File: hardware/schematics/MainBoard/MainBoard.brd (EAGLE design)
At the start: 80 x 107.6 mm, 17 parts

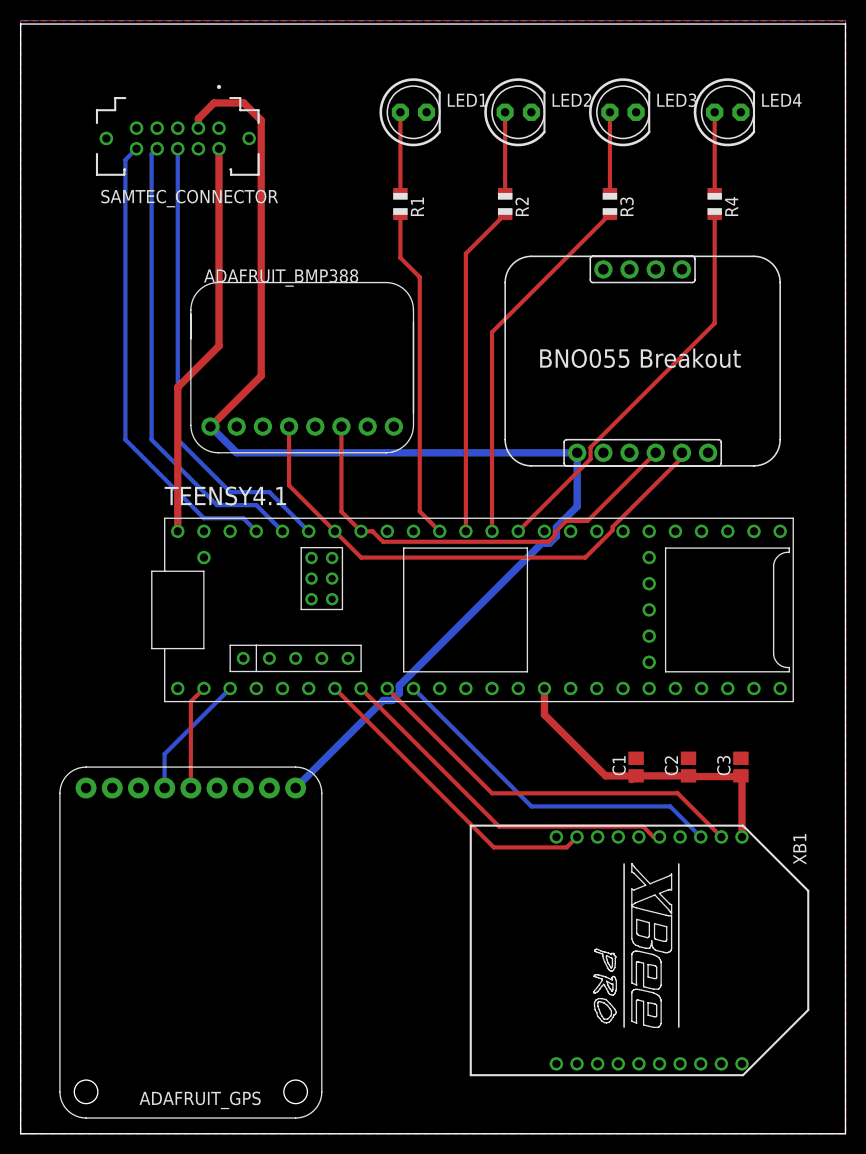
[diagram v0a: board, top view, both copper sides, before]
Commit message: Add Power Board | Change MB Connector Pins | Move Old PDB.sch to PCBs Folder
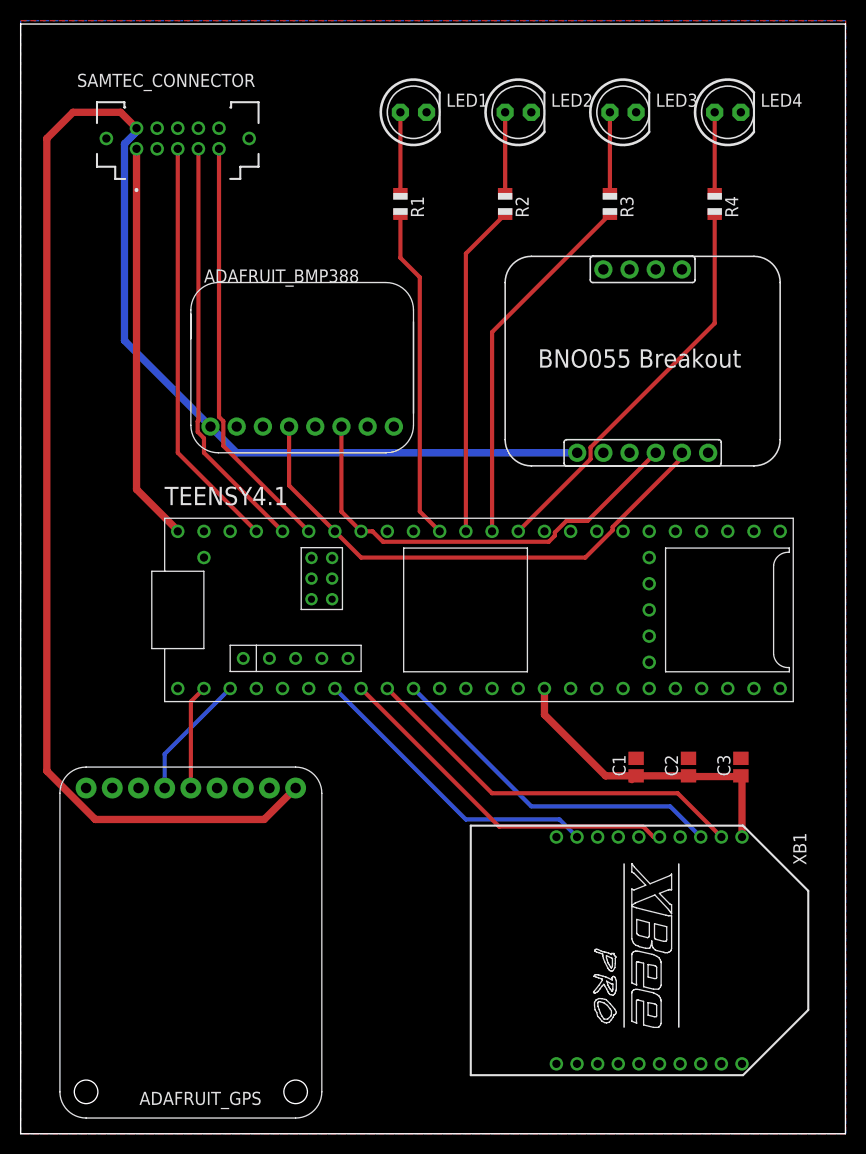
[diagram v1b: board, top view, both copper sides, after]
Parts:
- turned SAMTEC_CONNECTOR to 0 degrees
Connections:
- net 3V3: now also SAMTEC_CONNECTOR.02; no longer SAMTEC_CONNECTOR.03
- net 5V: now also SAMTEC_CONNECTOR.01; no longer SAMTEC_CONNECTOR.02
- net BATT_TEMP: now also SAMTEC_CONNECTOR.05, TEENSY4.1.D23/A9; no longer SAMTEC_CONNECTOR.06, TEENSY4.1.D21/A7
- net GND: now also SAMTEC_CONNECTOR.03, SAMTEC_CONNECTOR.06, SAMTEC_CONNECTOR.08, SAMTEC_CONNECTOR.10; no longer SAMTEC_CONNECTOR.01, SAMTEC_CONNECTOR.05, SAMTEC_CONNECTOR.07, SAMTEC_CONNECTOR.09
- net I_SENSE: now also SAMTEC_CONNECTOR.09, TEENSY4.1.D21/A7; no longer SAMTEC_CONNECTOR.08, TEENSY4.1.D22/A8
- net V_BATT: now also SAMTEC_CONNECTOR.07, TEENSY4.1.D22/A8; no longer SAMTEC_CONNECTOR.10, TEENSY4.1.D23/A9
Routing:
- net 3V3: track 153.2 -> 200.3 mm
- net V_BATT: track 45.0 -> 40.5 mm
- net BATT_TEMP: track 44.6 -> 40.3 mm
- net I_SENSE: track 44.8 -> 40.7 mm
- net XBEE_EN: track 30.3 -> 29.4 mm
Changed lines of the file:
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@@
 <drawing>
 <settings>
-<setting alwaysvectorfont="yes"/>
+<setting alwaysvectorfont="no"/>
 <setting verticaltext="up"/>
 </settings>
@@
 <attribute name="VALUE" x="20.066" y="5.842" size="1.27" layer="27" rot="R180"/>
 </element>
-<element name="SAMTEC_CONNECTOR" library="T2M-105-01-X-D-TH-WT" package="SAMTEC_T2M-105-01-X-D-TH-WT" value="T2M-105-01-X-D-TH-WT" x="15.24" y="96.52" smashed="yes" rot="R180">
-<attribute name="MANUFACTURER" value="Samtec" x="-39.37" y="166.37" size="1.778" layer="27" rot="R180" display="off"/>
-<attribute name="MAXIMUM_PACKAGE_HEIGHT" value="6.55mm" x="-39.37" y="166.37" size="1.778" layer="27" rot="R180" display="off"/>
-<attribute name="NAME" x="25.01" y="91.52" size="1.27" layer="25" rot="R180"/>
-<attribute name="PARTREV" value="AH" x="-39.37" y="166.37" size="1.778" layer="27" rot="R180" display="off"/>
-<attribute name="STANDARD" value="Manufacturer Recommendations" x="-39.37" y="166.37" size="1.778" layer="27" rot="R180" display="off"/>
-<attribute name="VALUE" x="23.74" y="102.02" size="1.27" layer="27" rot="R180" align="top-left"/>
+<element name="SAMTEC_CONNECTOR" library="T2M-105-01-X-D-TH-WT" package="SAMTEC_T2M-105-01-X-D-TH-WT" value="T2M-105-01-X-D-TH-WT" x="15.24" y="96.52" smashed="yes">
+<attribute name="MANUFACTURER" value="Samtec" x="69.85" y="26.67" size="1.778" layer="27" display="off"/>
+<attribute name="MAXIMUM_PACKAGE_HEIGHT" value="6.55mm" x="69.85" y="26.67" size="1.778" layer="27" display="off"/>
+<attribute name="NAME" x="5.47" y="101.52" size="1.27" layer="25"/>
+<attribute name="PARTREV" value="AH" x="69.85" y="26.67" size="1.778" layer="27" display="off"/>
+<attribute name="STANDARD" value="Manufacturer Recommendations" x="69.85" y="26.67" size="1.778" layer="27" display="off"/>
+<attribute name="VALUE" x="6.74" y="91.02" size="1.27" layer="27" align="top-left"/>
 </element>
 <element name="LED1" library="adafruit(seeIMUBreakout)" package="LED5MM" value="" x="38.1" y="99.06" smashed="yes">
@@
 <vertex x="0" y="0"/>
 </polygon>
-<contactref element="SAMTEC_CONNECTOR" pad="05"/>
-<contactref element="SAMTEC_CONNECTOR" pad="09"/>
-<contactref element="SAMTEC_CONNECTOR" pad="07"/>
-<contactref element="SAMTEC_CONNECTOR" pad="01"/>
+<contactref element="SAMTEC_CONNECTOR" pad="06"/>
+<contactref element="SAMTEC_CONNECTOR" pad="08"/>
+<contactref element="SAMTEC_CONNECTOR" pad="10"/>
+<contactref element="SAMTEC_CONNECTOR" pad="03"/>
 </signal>
 <signal name="AGND">
@@
 <signal name="5V">
 <contactref element="TEENSY4.1" pad="5V"/>
-<contactref element="SAMTEC_CONNECTOR" pad="02"/>
 <contactref element="TEENSY4.1" pad="VIN"/>
-<wire x1="19.24" y1="95.52" x2="19.24" y2="76.39" width="0.7112" layer="1"/>
-<wire x1="15.24" y1="72.39" x2="15.24" y2="58.42" width="0.7112" layer="1"/>
-<wire x1="19.24" y1="76.39" x2="15.24" y2="72.39" width="0.7112" layer="1"/>
+<contactref element="SAMTEC_CONNECTOR" pad="01"/>
+<wire x1="11.24" y1="95.52" x2="11.24" y2="62.5" width="0.7112" layer="1"/>
+<wire x1="15.24" y1="58.5" x2="11.24" y2="62.5" width="0.7112" layer="1"/>
+<wire x1="15.24" y1="58.5" x2="15.24" y2="58.42" width="0.7112" layer="1"/>
 <wire x1="21.59" y1="46.1" x2="15.24" y2="58.42" width="0" layer="19" extent="1-1"/>
 </signal>
@@
 <wire x1="64.77" y1="34.71" x2="59.69" y2="34.71" width="0.7112" layer="1"/>
 <wire x1="59.69" y1="34.71" x2="56.73" y2="34.71" width="0.7112" layer="1"/>
-<contactref element="SAMTEC_CONNECTOR" pad="03"/>
 <contactref element="U$1" pad="VIN"/>
-<wire x1="18.7559875" y1="99.9585" x2="17.24" y2="98.4425125" width="0.7112" layer="1"/>
-<wire x1="17.24" y1="97.52" x2="17.24" y2="98.4425125" width="0.7112" layer="1"/>
-<wire x1="18.7559875" y1="99.9585" x2="21.6490125" y2="99.9585" width="0.7112" layer="1"/>
-<wire x1="21.6490125" y1="99.9585" x2="23.3335" y2="98.2740125" width="0.7112" layer="1"/>
-<wire x1="23.3335" y1="98.2740125" x2="23.3335" y2="73.4985" width="0.7112" layer="1"/>
-<wire x1="18.415" y1="68.58" x2="23.3335" y2="73.4985" width="0.7112" layer="1"/>
-<wire x1="18.415" y1="68.58" x2="20.955" y2="66.04" width="0.7112" layer="16"/>
-<wire x1="20.955" y1="66.04" x2="53.975" y2="66.04" width="0.7112" layer="16"/>
 <contactref element="TEENSY4.1" pad="3.3V"/>
 <wire x1="50.8" y1="43.18" x2="50.8" y2="40.64" width="0.7112" layer="1"/>
 <wire x1="56.73" y1="34.71" x2="50.8" y2="40.64" width="0.7112" layer="1"/>
-<wire x1="53.975" y1="60.833" x2="53.975" y2="66.04" width="0.7112" layer="16"/>
-<wire x1="26.67" y1="33.528" x2="35.16" y2="42.018" width="0.7112" layer="16"/>
-<wire x1="35.16" y1="42.018" x2="36.04131875" y2="42.018" width="0.7112" layer="16"/>
-<wire x1="36.04131875" y1="42.018" x2="36.722" y2="42.69868125" width="0.7112" layer="16"/>
-<wire x1="51.28131875" y1="57.258" x2="51.962" y2="57.93868125" width="0.7112" layer="16"/>
-<wire x1="51.962" y1="57.93868125" x2="51.962" y2="58.82" width="0.7112" layer="16"/>
-<wire x1="51.962" y1="58.82" x2="53.975" y2="60.833" width="0.7112" layer="16"/>
-<wire x1="36.722" y1="42.69868125" x2="36.722" y2="43.44531875" width="0.7112" layer="16"/>
-<wire x1="36.722" y1="43.44531875" x2="50.53468125" y2="57.258" width="0.7112" layer="16"/>
-<wire x1="50.53468125" y1="57.258" x2="51.28131875" y2="57.258" width="0.7112" layer="16"/>
+<contactref element="SAMTEC_CONNECTOR" pad="02"/>
+<wire x1="11.24" y1="97.52" x2="9.7" y2="99.06" width="0.7112" layer="1"/>
+<wire x1="9.7" y1="99.06" x2="5.08" y2="99.06" width="0.7112" layer="1"/>
+<wire x1="2.54" y1="96.52" x2="5.08" y2="99.06" width="0.7112" layer="1"/>
+<wire x1="26.67" y1="33.528" x2="23.622" y2="30.48" width="0.7112" layer="1"/>
+<wire x1="7.2427375" y1="30.48" x2="2.54" y2="35.1827375" width="0.7112" layer="1"/>
+<wire x1="2.54" y1="35.1827375" x2="2.54" y2="96.52" width="0.7112" layer="1"/>
+<wire x1="23.622" y1="30.48" x2="7.2427375" y2="30.48" width="0.7112" layer="1"/>
+<wire x1="11.24" y1="97.52" x2="11.24" y2="97.1725125" width="0.7112" layer="16"/>
+<wire x1="11.24" y1="97.1725125" x2="10.0715" y2="96.0040125" width="0.7112" layer="16"/>
+<wire x1="10.0715" y1="96.0040125" x2="10.0715" y2="76.9235" width="0.7112" layer="16"/>
+<wire x1="10.0715" y1="76.9235" x2="18.415" y2="68.58" width="0.7112" layer="16"/>
+<wire x1="18.415" y1="68.58" x2="20.955" y2="66.04" width="0.7112" layer="16"/>
+<wire x1="20.955" y1="66.04" x2="53.975" y2="66.04" width="0.7112" layer="16"/>
 <wire x1="53.975" y1="66.04" x2="50.8" y2="43.18" width="0" layer="19" extent="1-1"/>
 </signal>
@@
 <contactref element="XB1" pad="9"/>
 <contactref element="TEENSY4.1" pad="D5"/>
-<wire x1="45.8896" y1="27.7704" x2="30.48" y2="43.18" width="0.4064" layer="1"/>
-<wire x1="53.96" y1="28.78" x2="52.9504" y2="27.7704" width="0.4064" layer="1"/>
-<wire x1="52.9504" y1="27.7704" x2="45.8896" y2="27.7704" width="0.4064" layer="1"/>
+<wire x1="30.48" y1="43.18" x2="43.18" y2="30.48" width="0.4064" layer="16"/>
+<wire x1="52.26" y1="30.48" x2="53.96" y2="28.78" width="0.4064" layer="16"/>
+<wire x1="43.18" y1="30.48" x2="52.26" y2="30.48" width="0.4064" layer="16"/>
 </signal>
 <signal name="N$8">
@@
 </signal>
 <signal name="V_BATT">
-<contactref element="TEENSY4.1" pad="D23/A9"/>
-<contactref element="SAMTEC_CONNECTOR" pad="10"/>
-<wire x1="10.16" y1="94.44" x2="11.24" y2="95.52" width="0.4064" layer="16"/>
-<wire x1="22.86" y1="58.42" x2="21.59" y2="59.69" width="0.4064" layer="16"/>
-<wire x1="21.59" y1="59.69" x2="17.78" y2="59.69" width="0.4064" layer="16"/>
-<wire x1="17.78" y1="59.69" x2="10.16" y2="67.31" width="0.4064" layer="16"/>
-<wire x1="10.16" y1="67.31" x2="10.16" y2="94.44" width="0.4064" layer="16"/>
+<contactref element="SAMTEC_CONNECTOR" pad="07"/>
+<contactref element="TEENSY4.1" pad="D22/A8"/>
+<wire x1="17.1704" y1="69.09553125" x2="17.1704" y2="68.06446875" width="0.4064" layer="1"/>
+<wire x1="17.1704" y1="68.06446875" x2="17.78" y2="67.45486875" width="0.4064" layer="1"/>
+<wire x1="17.78" y1="67.45486875" x2="17.78" y2="66.04" width="0.4064" layer="1"/>
+<wire x1="17.24" y1="95.52" x2="17.24" y2="69.16513125" width="0.4064" layer="1"/>
+<wire x1="17.24" y1="69.16513125" x2="17.1704" y2="69.09553125" width="0.4064" layer="1"/>
+<wire x1="17.78" y1="66.04" x2="25.4" y2="58.42" width="0.4064" layer="1"/>
 </signal>
 <signal name="SDA">
@@
 </signal>
 <signal name="I_SENSE">
-<contactref element="TEENSY4.1" pad="D22/A8"/>
-<contactref element="SAMTEC_CONNECTOR" pad="08"/>
-<wire x1="25.4" y1="58.42" x2="22.86" y2="60.96" width="0.4064" layer="16"/>
-<wire x1="19.05" y1="60.96" x2="12.7" y2="67.31" width="0.4064" layer="16"/>
-<wire x1="12.7" y1="67.31" x2="12.7" y2="94.98" width="0.4064" layer="16"/>
-<wire x1="12.7" y1="94.98" x2="13.24" y2="95.52" width="0.4064" layer="16"/>
-<wire x1="22.86" y1="60.96" x2="19.05" y2="60.96" width="0.4064" layer="16"/>
+<contactref element="SAMTEC_CONNECTOR" pad="09"/>
+<contactref element="TEENSY4.1" pad="D21/A7"/>
+<wire x1="19.6596" y1="69.09553125" x2="19.24" y2="69.51513125" width="0.4064" layer="1"/>
+<wire x1="19.24" y1="69.51513125" x2="19.24" y2="95.52" width="0.4064" layer="1"/>
+<wire x1="27.94" y1="58.42" x2="19.6596" y2="66.7004" width="0.4064" layer="1"/>
+<wire x1="19.6596" y1="66.7004" x2="19.6596" y2="69.09553125" width="0.4064" layer="1"/>
 </signal>
 <signal name="BATT_TEMP">
-<contactref element="TEENSY4.1" pad="D21/A7"/>
-<contactref element="SAMTEC_CONNECTOR" pad="06"/>
-<wire x1="15.24" y1="95.52" x2="15.24" y2="67.31" width="0.4064" layer="16"/>
-<wire x1="15.24" y1="67.31" x2="20.32" y2="62.23" width="0.4064" layer="16"/>
-<wire x1="24.13" y1="62.23" x2="27.94" y2="58.42" width="0.4064" layer="16"/>
-<wire x1="20.32" y1="62.23" x2="24.13" y2="62.23" width="0.4064" layer="16"/>
+<contactref element="SAMTEC_CONNECTOR" pad="05"/>
+<contactref element="TEENSY4.1" pad="D23/A9"/>
+<wire x1="15.24" y1="66.04" x2="22.86" y2="58.42" width="0.4064" layer="1"/>
+<wire x1="15.24" y1="95.52" x2="15.24" y2="66.04" width="0.4064" layer="1"/>
 </signal>
 </signals>
